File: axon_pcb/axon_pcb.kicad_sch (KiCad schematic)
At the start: 108 parts, among them J1 USB_C_Receptacle, J2 AVR_ISP Header, K1 KEYSW, K10 KEYSW, K11 KEYSW, K12 KEYSW, K13 KEYSW, K14 KEYSW, K15 KEYSW, K16 KEYSW, K17 KEYSW, K18 KEYSW, K19 KEYSW, K2 KEYSW, K20 KEYSW, K21 KEYSW, K22 KEYSW, K23 KEYSW, K24 KEYSW, K25 KEYSW, K26 KEYSW, K27 KEYSW, K28 KEYSW, K29 KEYSW, K3 KEYSW, K30 KEYSW, K31 KEYSW, K32 KEYSW, K33 KEYSW, K34 KEYSW, K35 KEYSW, K36 KEYSW, K37 KEYSW, K38 KEYSW, K39 KEYSW, K4 KEYSW, K40 KEYSW, K41 KEYSW, K42 KEYSW, K43 KEYSW, K44 KEYSW, K45 KEYSW, K46 KEYSW, K5 KEYSW, K6 KEYSW, K7 KEYSW, K8 KEYSW, K9 KEYSW, SW1 RESET, SW2 BOOT, U1 ATmega328P-PU, X1 16MHz

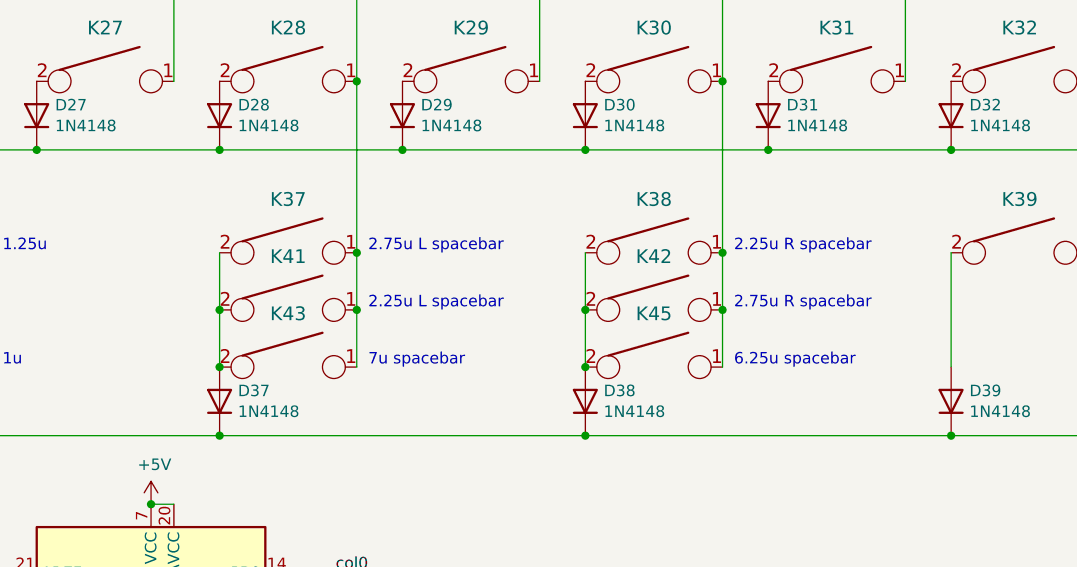
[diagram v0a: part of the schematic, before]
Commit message: change rear silk to show keyswitch numbers
and make the schematic a little neater
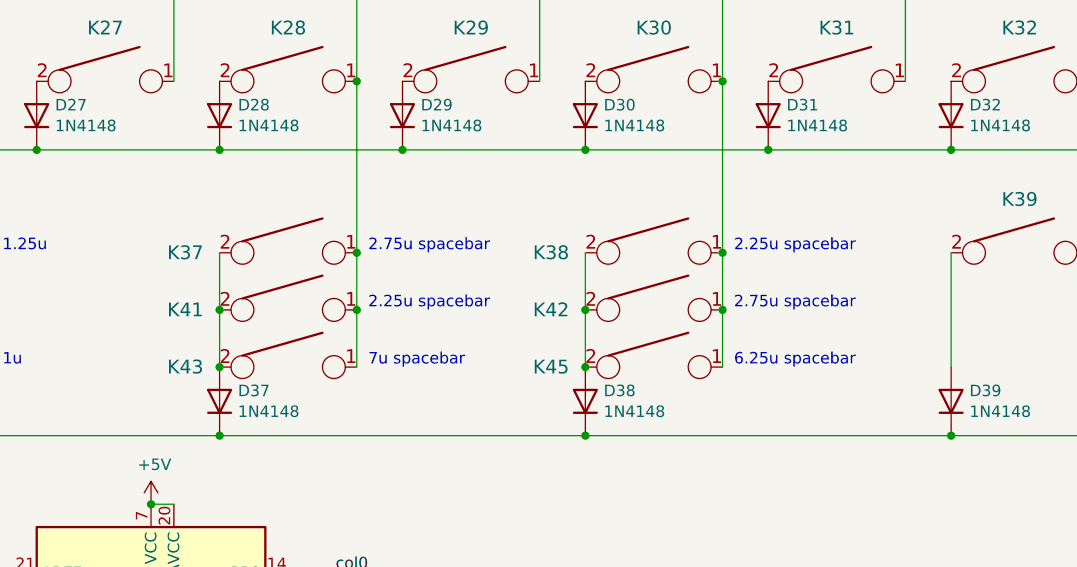
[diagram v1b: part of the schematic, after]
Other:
- note added: "2.25u spacebar"
- note added: "2.75u spacebar"
- note removed: "2.25u L spacebar"
- note removed: "2.25u R spacebar"
- note removed: "2.75u L spacebar"
- note removed: "2.75u R spacebar"
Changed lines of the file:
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@@
     (effects (font (size 1.27 1.27)) (justify left bottom))
   )
-  (text "2.75u R spacebar" (at 171.45 93.98 0)
-    (effects (font (size 1.27 1.27)) (justify left bottom))
-  )
-  (text "2.75u L spacebar" (at 130.81 87.63 0)
+  (text "2.75u spacebar" (at 171.45 93.98 0)
+    (effects (font (size 1.27 1.27)) (justify left bottom))
+  )
+  (text "2.75u spacebar" (at 130.81 87.63 0)
     (effects (font (size 1.27 1.27)) (justify left bottom))
   )
@@
     (effects (font (size 1.27 1.27)) (justify left bottom))
   )
-  (text "2.25u R spacebar" (at 171.45 87.63 0)
+  (text "2.25u spacebar" (at 171.45 87.63 0)
     (effects (font (size 1.27 1.27)) (justify left bottom))
   )
@@
     (effects (font (size 1.27 1.27)) (justify left bottom))
   )
-  (text "2.25u L spacebar" (at 130.81 93.98 0)
+  (text "2.25u spacebar" (at 130.81 93.98 0)
     (effects (font (size 1.27 1.27)) (justify left bottom))
   )
@@
   (symbol (lib_id "keyboard-parts:KEYSW") (at 121.92 87.63 0) (unit 1)
     (in_bom yes) (on_board yes)
-    (property "Reference" "K37" (id 0) (at 121.92 81.7118 0)
+    (property "Reference" "K37" (id 0) (at 110.49 87.63 0)
       (effects (font (size 1.524 1.524)))
     )
@@
   (symbol (lib_id "keyboard-parts:KEYSW") (at 162.56 87.63 0) (unit 1)
     (in_bom yes) (on_board yes)
-    (property "Reference" "K38" (id 0) (at 162.56 81.7118 0)
+    (property "Reference" "K38" (id 0) (at 151.13 87.63 0)
       (effects (font (size 1.524 1.524)))
     )
@@
   (symbol (lib_id "keyboard-parts:KEYSW") (at 121.92 93.98 0) (unit 1)
     (in_bom yes) (on_board yes)
-    (property "Reference" "K41" (id 0) (at 121.92 88.0618 0)
+    (property "Reference" "K41" (id 0) (at 110.49 93.98 0)
       (effects (font (size 1.524 1.524)))
     )
@@
   (symbol (lib_id "keyboard-parts:KEYSW") (at 162.56 93.98 0) (unit 1)
     (in_bom yes) (on_board yes)
-    (property "Reference" "K42" (id 0) (at 162.56 88.0618 0)
+    (property "Reference" "K42" (id 0) (at 151.13 93.98 0)
       (effects (font (size 1.524 1.524)))
     )
@@
   (symbol (lib_id "keyboard-parts:KEYSW") (at 162.56 100.33 0) (unit 1)
     (in_bom yes) (on_board yes)
-    (property "Reference" "K45" (id 0) (at 162.56 94.4118 0)
+    (property "Reference" "K45" (id 0) (at 151.13 100.33 0)
       (effects (font (size 1.524 1.524)))
     )
@@
   (symbol (lib_id "keyboard-parts:KEYSW") (at 121.92 100.33 0) (unit 1)
     (in_bom yes) (on_board yes)
-    (property "Reference" "K43" (id 0) (at 121.92 94.4118 0)
-      (effects (font (size 1.524 1.524)))
-    )
+    (property "Reference" "K43" (id 0) (at 110.49 100.33 0)
+      (effects (font (size 1.524 1.524)))
+    )

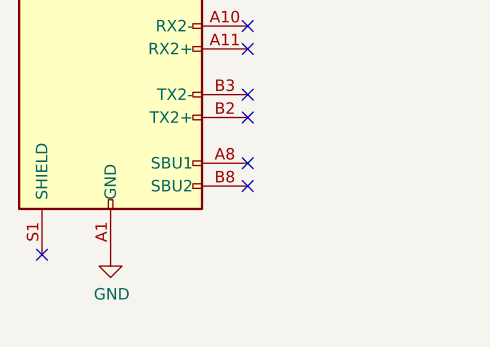
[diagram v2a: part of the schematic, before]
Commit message: connect shield to ground
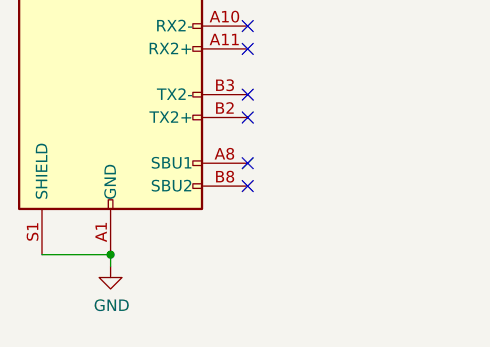
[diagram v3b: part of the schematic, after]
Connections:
- net GND: now also J1.S1 (SHIELD)
- no-connect marks 12 -> 11
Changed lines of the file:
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@@
   (junction (at 170.18 93.98) (diameter 0) (color 0 0 0 0)
+  )
+  (junction (at 27.94 189.23) (diameter 0) (color 0 0 0 0)
   )
   (junction (at 129.54 87.63) (diameter 0) (color 0 0 0 0)
@@
   (no_connect (at 43.18 151.13))
   (no_connect (at 43.18 166.37))
-  (no_connect (at 20.32 189.23))
   (no_connect (at 43.18 156.21))
   (no_connect (at 91.44 123.19))
@@
     (stroke (width 0) (type default) (color 0 0 0 0))
   )
+  (wire (pts (xy 27.94 189.23) (xy 27.94 190.5))
+    (stroke (width 0) (type default) (color 0 0 0 0))
+  )
   (wire (pts (xy 271.78 40.64) (xy 271.78 49.53))
     (stroke (width 0) (type default) (color 0 0 0 0))
@@
   )
   (wire (pts (xy 59.69 142.24) (xy 59.69 143.51))
+    (stroke (width 0) (type default) (color 0 0 0 0))
+  )
+  (wire (pts (xy 20.32 189.23) (xy 27.94 189.23))
     (stroke (width 0) (type default) (color 0 0 0 0))
   )
@@
     (pin "2")
   )
-  (symbol (lib_id "power:GND") (at 27.94 189.23 0) (unit 1)
-    (in_bom yes) (on_board yes)
-    (property "Reference" "#PWR0101" (id 0) (at 27.94 195.58 0)
-      (effects (font (size 1.27 1.27)) hide)
-    )
-    (property "Value" "GND" (id 1) (at 28.067 193.6242 0))
-    (property "Footprint" "" (id 2) (at 27.94 189.23 0)
-      (effects (font (size 1.27 1.27)) hide)
-    )
-    (property "Datasheet" "" (id 3) (at 27.94 189.23 0)
-      (effects (font (size 1.27 1.27)) hide)
-    )
+  (symbol (lib_id "power:GND") (at 27.94 190.5 0) (unit 1)
+    (in_bom yes) (on_board yes)
+    (property "Reference" "#PWR0101" (id 0) (at 27.94 196.85 0)
+      (effects (font (size 1.27 1.27)) hide)
+    )
+    (property "Value" "GND" (id 1) (at 28.067 194.8942 0))
+    (property "Footprint" "" (id 2) (at 27.94 190.5 0)
+      (effects (font (size 1.27 1.27)) hide)
+    )
+    (property "Datasheet" "" (id 3) (at 27.94 190.5 0)
+      (effects (font (size 1.27 1.27)) hide)
+    )

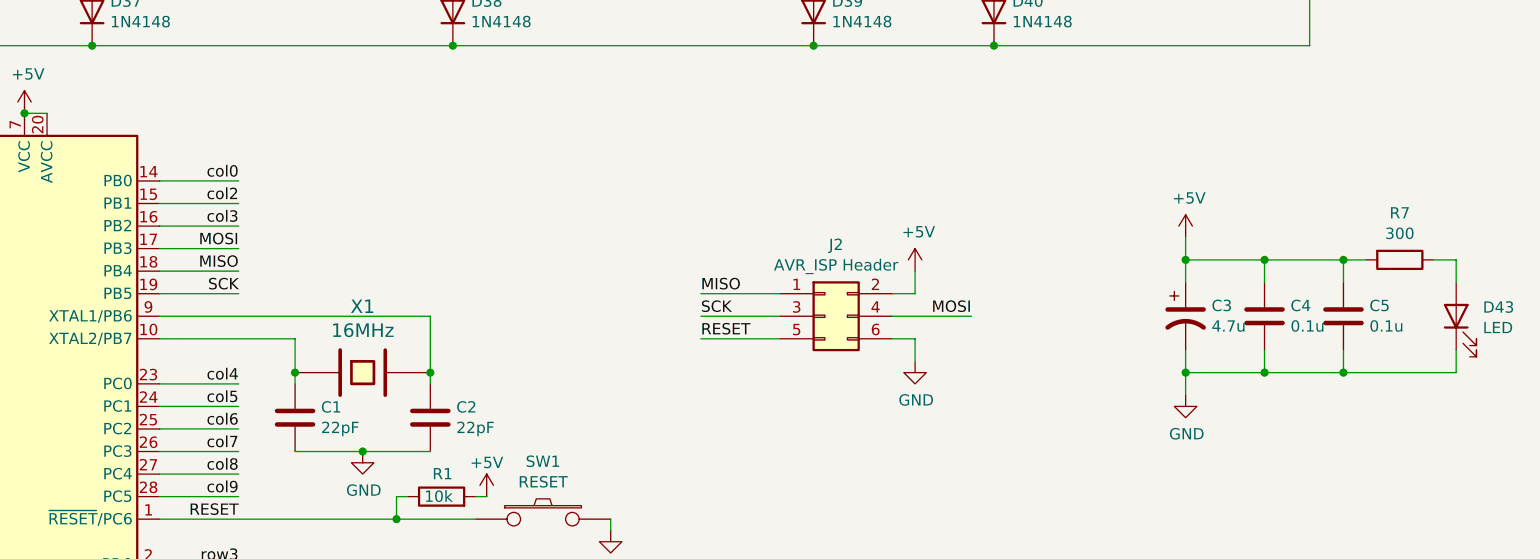
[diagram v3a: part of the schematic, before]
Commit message: adjust diode footprint, and LED connection
- diode footprint changed to prettier symbol
- LED now software-controlled
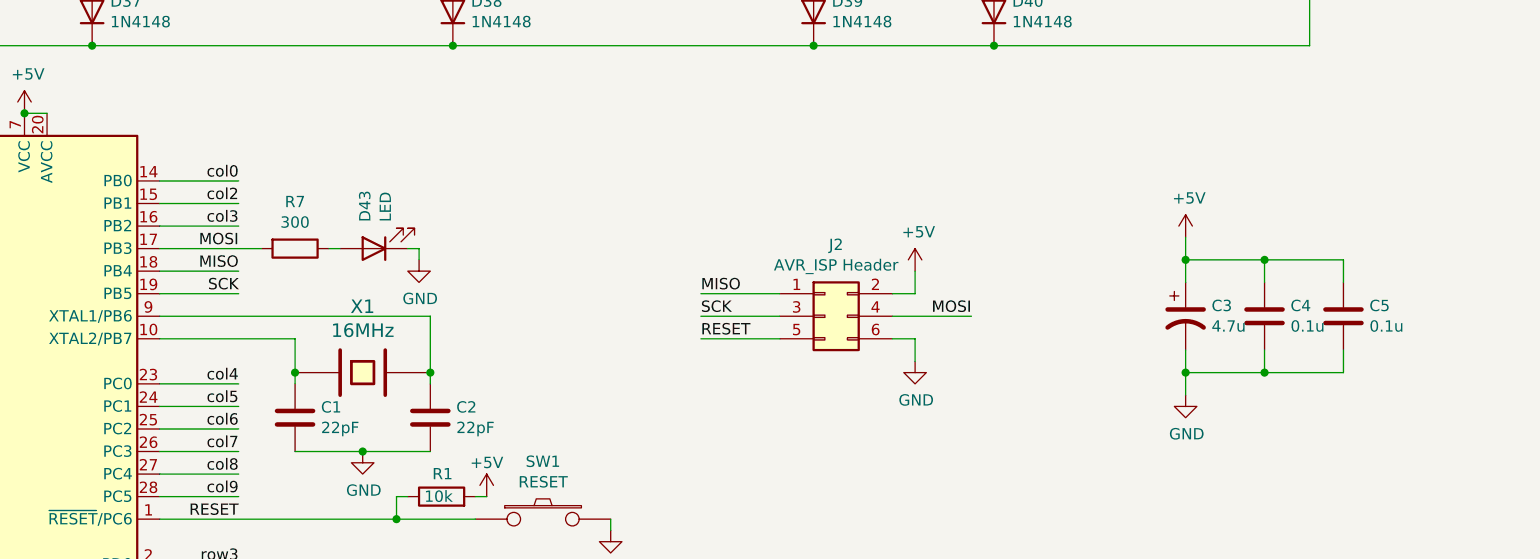
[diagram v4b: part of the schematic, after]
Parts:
- D1, D10, D11, D12, D13, D14, D15, D16, D17, D18, D19, D2, D20, D21, D22, D23, D24, D25, D26, D27, D28, D29, D3, D30, D31, D32, D33, D34, D35, D36, D37, D38, D39, D4, D40, D41, D42, D5, D6, D7, D8, D9: footprint Diode_THT:D_DO-35_SOD27_P7.62mm_Horizontal -> personal:D_DO-35_SOD27_P7.62mm_Horizontal_personal
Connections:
- net +5V: no longer R7.2
- net MOSI: now also R7.2
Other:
- moved on the sheet: D43, R7
